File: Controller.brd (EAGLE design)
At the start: 35.6 x 22.9 mm, 18 parts, among them IC1 PIC16F1826/27SO, X1 057-010-1

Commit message: Updates
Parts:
- added C3: (no value), resistor:C1206
- renumbered JP1 to CS0, JP2 to CS1, JP3 to CS2, JP4 to CS3
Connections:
- net +5V: now also C3.1
- net GND: now also C3.2
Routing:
- net +5V: track 33.1 -> 37.2 mm
- net GND: track 56.2 -> 58.0 mm
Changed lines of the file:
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@@
 <attribute name="OC_FARNELL" value="unknown" x="25.4" y="11.43" size="1.778" layer="27" rot="R270" display="off"/>
 </element>
-<element name="JP1" library="SparkFun-Jumpers" package="SMT-JUMPER_2_NO_SILK" value="JUMPER-SMT_2_NO_SILK" x="31.115" y="17.78" smashed="yes" rot="R180">
+<element name="CS0" library="SparkFun-Jumpers" package="SMT-JUMPER_2_NO_SILK" value="JUMPER-SMT_2_NO_SILK" x="31.115" y="17.78" smashed="yes" rot="R180">
 <attribute name="NAME" x="33.655" y="17.907" size="0.6096" layer="25" font="vector" ratio="20" rot="R180" align="bottom-center"/>
 </element>
-<element name="JP2" library="SparkFun-Jumpers" package="SMT-JUMPER_2_NO_SILK" value="JUMPER-SMT_2_NO_SILK" x="31.115" y="15.24" smashed="yes" rot="R180">
+<element name="CS1" library="SparkFun-Jumpers" package="SMT-JUMPER_2_NO_SILK" value="JUMPER-SMT_2_NO_SILK" x="31.115" y="15.24" smashed="yes" rot="R180">
 <attribute name="NAME" x="33.655" y="15.367" size="0.6096" layer="25" font="vector" ratio="20" rot="R180" align="bottom-center"/>
 </element>
-<element name="JP3" library="SparkFun-Jumpers" package="SMT-JUMPER_2_NO_SILK" value="JUMPER-SMT_2_NO_SILK" x="31.115" y="12.7" smashed="yes" rot="R180">
+<element name="CS2" library="SparkFun-Jumpers" package="SMT-JUMPER_2_NO_SILK" value="JUMPER-SMT_2_NO_SILK" x="31.115" y="12.7" smashed="yes" rot="R180">
 <attribute name="NAME" x="33.655" y="12.827" size="0.6096" layer="25" font="vector" ratio="20" rot="R180" align="bottom-center"/>
 </element>
-<element name="JP4" library="SparkFun-Jumpers" package="SMT-JUMPER_2_NO_SILK" value="JUMPER-SMT_2_NO_SILK" x="31.115" y="10.16" smashed="yes" rot="R180">
+<element name="CS3" library="SparkFun-Jumpers" package="SMT-JUMPER_2_NO_SILK" value="JUMPER-SMT_2_NO_SILK" x="31.115" y="10.16" smashed="yes" rot="R180">
 <attribute name="NAME" x="33.655" y="10.287" size="0.6096" layer="25" font="vector" ratio="20" rot="R180" align="bottom-center"/>
 </element>
@@
 <attribute name="VALUE" x="26.67" y="6.35" size="1.27" layer="28" rot="MR180"/>
 </element>
+<element name="C3" library="resistor" package="C1206" value="" x="10.16" y="12.7" smashed="yes" rot="R90">
+<attribute name="VALUE" x="12.7" y="11.43" size="1.27" layer="27" rot="R90"/>
+</element>
 </elements>
 <signals>
@@
 <wire x1="21.59" y1="13.97" x2="20.0279" y2="13.97" width="0.4064" layer="16"/>
 <via x="15.24" y="15.875" extent="1-16" drill="0.5"/>
-<wire x1="15.24" y1="15.875" x2="6.35" y2="15.875" width="0.4064" layer="1"/>
+<wire x1="15.24" y1="15.875" x2="10.16" y2="15.875" width="0.4064" layer="1"/>
 <via x="6.35" y="15.875" extent="1-16" drill="0.5"/>
 <contactref element="JPGND" pad="1"/>
+<wire x1="10.16" y1="15.875" x2="6.35" y2="15.875" width="0.4064" layer="1"/>
 <wire x1="15.24" y1="11.2014" x2="15.24" y2="12.7" width="0.4064" layer="1"/>
 <via x="15.24" y="12.7" extent="1-16" drill="0.5"/>
@@
 <wire x1="1.775" y1="15.875" x2="1.775" y2="17.145" width="0.4064" layer="16"/>
 <wire x1="6.35" y1="15.875" x2="1.775" y2="15.875" width="0.4064" layer="16"/>
+<contactref element="C3" pad="2"/>
+<wire x1="10.16" y1="14.1" x2="10.16" y2="15.875" width="0.4064" layer="1"/>
 </signal>
 <signal name="+5V">
@@
 <wire x1="31.75" y1="7.62" x2="30.48" y2="7.62" width="0.4064" layer="16"/>
 <wire x1="30.48" y1="7.62" x2="26.67" y2="11.43" width="0.4064" layer="16"/>
+<contactref element="C3" pad="1"/>
+<wire x1="10.16" y1="11.3" x2="11.3" y2="11.3" width="0.4064" layer="1"/>
+<wire x1="11.3" y1="11.3" x2="12.065" y2="12.065" width="0.4064" layer="1"/>
+<wire x1="12.065" y1="12.065" x2="12.065" y2="13.97" width="0.4064" layer="1"/>
 </signal>
 <signal name="N$1">
@@
 </signal>
 <signal name="N$4">
-<contactref element="JP1" pad="1"/>
-<contactref element="JP2" pad="1"/>
-<contactref element="JP3" pad="1"/>
-<contactref element="JP4" pad="1"/>
+<contactref element="CS0" pad="1"/>
+<contactref element="CS1" pad="1"/>
+<contactref element="CS2" pad="1"/>
+<contactref element="CS3" pad="1"/>
 <contactref element="IC1" pad="11"/>
 <wire x1="31.5214" y1="17.78" x2="31.5214" y2="15.24" width="0.4064" layer="1"/>
@@
 </signal>
 <signal name="N$5">
-<contactref element="JP1" pad="2"/>
+<contactref element="CS0" pad="2"/>
 <contactref element="X1" pad="2"/>
 <wire x1="26.67" y1="16.51" x2="29.4386" y2="16.51" width="0.4064" layer="1"/>
@@
 </signal>
 <signal name="N$6">
-<contactref element="JP2" pad="2"/>
+<contactref element="CS1" pad="2"/>
 <contactref element="X1" pad="4"/>
 <wire x1="26.67" y1="13.97" x2="29.4386" y2="13.97" width="0.4064" layer="1"/>
@@
 </signal>
 <signal name="N$7">
-<contactref element="JP3" pad="2"/>
+<contactref element="CS2" pad="2"/>
 <contactref element="X1" pad="8"/>
 <wire x1="26.67" y1="8.89" x2="27.94" y2="10.16" width="0.4064" layer="1"/>
@@
 </signal>
 <signal name="N$8">
-<contactref element="JP4" pad="2"/>
+<contactref element="CS3" pad="2"/>
 <contactref element="X1" pad="10"/>
 <wire x1="30.7086" y1="10.16" x2="30.7086" y2="9.1186" width="0.4064" layer="1"/>

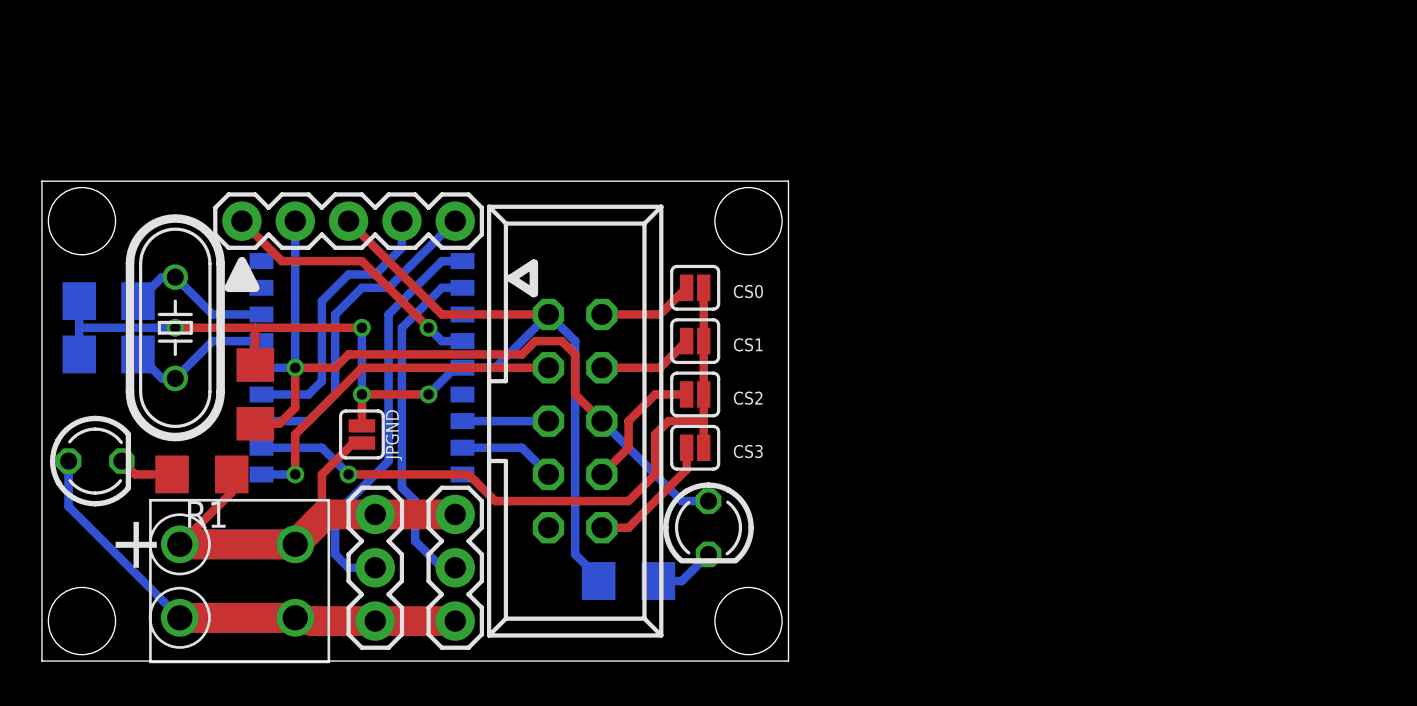
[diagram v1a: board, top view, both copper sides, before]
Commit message: Updated design to include 5V power supply
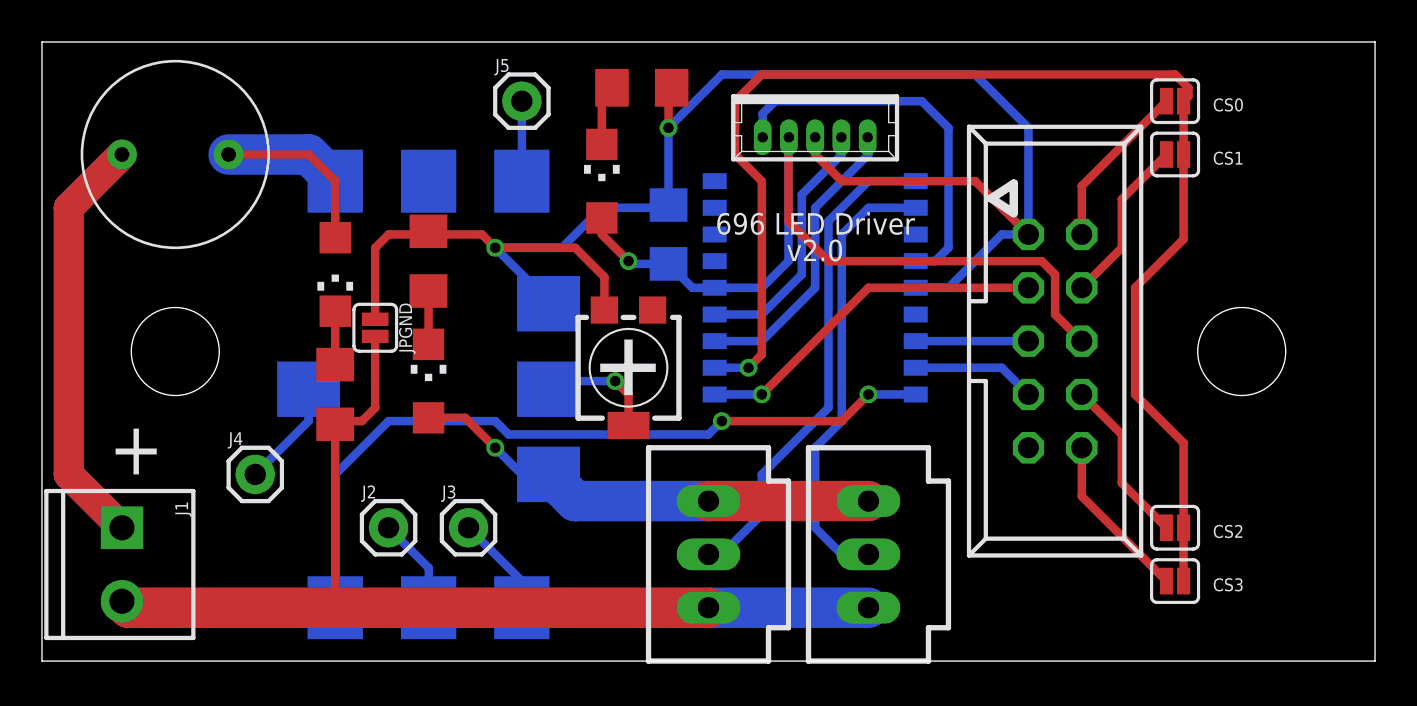
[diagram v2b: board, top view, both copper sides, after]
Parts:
- removed C1, C2: (no value), resistor:C1206
- removed Q1: (no value), crystal:HC49/S
- removed U$1: LSF-023.5, FRC696:LSF-3.5
- added J4, J5: (no value), SparkFun-Connectors:1X01
- added LED3: (no value), led:CHIPLED_1206
- added R3: (no value), resistor:RTRIM4G/J
- added R4: (no value), resistor:R1206
- added U$2: OKL2-T12-W12, FRC696:OKL2
- added U$3: 0034.6081, JSB2:MSF250
- added X2, X3: C-GRID-03-70543, con-molex:70543-03
- added X4: 53047-05, con-molex:53047-05
- J1: device SparkFun-Connectors:1X03 -> SparkFun-Connectors:SCREWTERMINAL-3.5MM-2
- J2: device SparkFun-Connectors:1X03 -> SparkFun-Connectors:1X01
- J3: device SparkFun-Connectors:1X05 -> SparkFun-Connectors:1X01
- LED1, LED2: device led:LED3MM -> led:CHIPLED_1206
- moved CS0 24.5 mm to (54.0, 26.7)
- moved CS1 24.5 mm to (54.0, 24.1)
- moved CS2 23.7 mm to (54.0, 6.35)
- moved CS3 23.7 mm to (54.0, 3.81)
- moved R2 23.5 mm to (28.6, 27.3), flipped to the top
- moved X1 23.2 mm to (48.3, 15.2)
- moved IC1 21.9 mm to (36.8, 17.8)
- moved C3 21.1 mm to (29.8, 20.3), flipped to the bottom
- moved J3 18.2 mm to (20.3, 6.35)
- moved LED2 17.3 mm to (26.7, 22.9), turned to 0 degrees
- moved LED1 14.5 mm to (14.0, 18.4), turned to 180 degrees
- moved J1 12.1 mm to (3.81, 6.35)
- moved R1 7.41 mm to (14.0, 12.7), turned to 90 degrees
- moved JPGND 5.12 mm to (15.9, 15.9)
- moved J2 3.24 mm to (16.5, 6.35), turned to 0 degrees
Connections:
- new net +5V/2: LED3.A, U$2.P$6, X2.3, X3.3
- new net N$19: R3.2, U$2.P$5
- new net N$20: J2.1, U$2.P$8
- new net N$21: J3.1, U$2.P$7
- new net N$22: J4.1, U$2.P$9
- new net N$23: IC1.9, U$2.P$1
- new net N$24: J5.1, U$2.P$3
- net +12V: now also U$2.P$2, U$3.P$1; no longer J1.3, J2.3, U$1.P$3
- net +5V: now also X4.2; no longer J3.2
- net GND: now also R3.3, R4.1, U$2.P$4, X4.3; no longer C1.2, C2.2, J3.3
- net N$10: now also LED3.C, R4.2; no longer C2.1, IC1.16, Q1.2
- net N$11: now also J1.2, X2.1, X3.1; no longer J1.1, J2.1, U$1.P$4
- net N$12: now also X2.2; no longer J1.2
- net N$13: now also X3.2; no longer J2.2
- net N$14: now also X4.1; no longer J3.1
- net N$15: now also X4.4; no longer J3.4
- net N$16: now also X4.5; no longer J3.5
- net N$17: now also LED1.C; no longer LED1.K
- net N$18: now also LED2.C; no longer LED2.K
- net N$9: now also J1.1, U$3.P$2; no longer C1.1, IC1.15, Q1.1
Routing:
- net N$23: track 0.00 -> 36.1 mm, vias 0 -> 2
- net N$9: track 7.09 -> 39.8 mm
- net N$11: track 17.5 -> 50.1 mm
- net N$4: track 32.4 -> 63.0 mm
- net +5V/2: track 0.00 -> 22.6 mm, vias 0 -> 1
- net GND: track 58.0 -> 78.9 mm, vias 4 -> 2
- net N$19: track 0.00 -> 5.71 mm, vias 0 -> 1
- net N$14: track 12.9 -> 18.3 mm, vias 1 -> 0
- net N$22: track 0.00 -> 5.11 mm
- net N$13: track 16.5 -> 21.6 mm
- net N$21: track 0.00 -> 4.86 mm
- net N$20: track 0.00 -> 4.60 mm
- net N$10: track 7.09 -> 2.54 mm
- net N$12: track 19.2 -> 23.6 mm
- net N$24: track 0.00 -> 3.81 mm
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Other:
- board size 35.6 x 22.9 mm -> 63.5 x 29.5 mm
- board text added: "696 LED Driver"
- board text added: "v2.0"

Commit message: Removing onboard voltage regulator
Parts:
- removed J2, J3, J4, J5: (no value), SparkFun-Connectors:1X01
- removed LED1: (no value), led:CHIPLED_1206
- removed R1: (no value), resistor:R1206
- removed R3: (no value), resistor:RTRIM4G/J
- removed U$2: OKL2-T12-W12, FRC696:OKL2
- moved J1 17.8 mm to (21.6, 6.35)
- moved U$3 14.0 mm to (20.3, 24.1)
- moved JPGND 12.5 mm to (26.7, 9.53)
- moved R4 11.4 mm to (28.6, 14.0), turned to 90 degrees
- moved LED3 7.65 mm to (26.0, 14.0)
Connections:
- removed net +12V: LED1.A, U$2.P$2, U$3.P$1
- removed net N$17: LED1.C, R1.2
- removed net N$19: R3.2, U$2.P$5
- removed net N$20: J2.1, U$2.P$8
- removed net N$21: J3.1, U$2.P$7
- removed net N$22: J4.1, U$2.P$9
- removed net N$23: IC1.9, U$2.P$1
- removed net N$24: J5.1, U$2.P$3
- net +5V/2: now also U$3.P$1; no longer U$2.P$6
- net GND: no longer R3.3, U$2.P$4
- net N$11: no longer R1.1
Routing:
- net N$23: track 36.1 -> 0.00 mm, vias 2 -> 0
- net N$11: track 50.1 -> 25.1 mm
- net +5V/2: track 22.6 -> 41.1 mm, vias 1 -> 0
- net +12V: track 13.9 -> 0.00 mm
- net GND: track 78.9 -> 67.9 mm, vias 2 -> 1
- net N$19: track 5.71 -> 0.00 mm, vias 1 -> 0
- net N$22: track 5.11 -> 0.00 mm
- net N$21: track 4.86 -> 0.00 mm
- net N$20: track 4.60 -> 0.00 mm
- net N$24: track 3.81 -> 0.00 mm
- net N$17: track 2.54 -> 0.00 mm
- net N$9: track 39.8 -> 38.4 mm
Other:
- board size 63.5 x 29.5 mm -> 43.2 x 29.5 mm
- board text added: "v2.1"
- board text removed: "v2.0"
